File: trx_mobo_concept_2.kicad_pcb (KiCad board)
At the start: 2 copper layers, 200 x 100 mm, 416 parts, among them J301 CONN_SMA_VERT, J302 CONN2, J303 CONN_SMA_VERT, J304 CONN3, J305 CONN_SMA_VERT, J306 CONN3, J307 CONN2, J308 CONN_SMA_VERT, J309 CONN8, Q1201 BSS138, Q1301 MMBT3904, Q1302 MMBT3904, Q1303 MMBT3904, Q1601 SI2369, Q1602 BSS138, Q1603 MMBT3904, Q1604 SI2369, Q1605 BSS138, Q1606 MMBT3904, Q1701 MMBT3906, Q1702 MMBT3904, Q1703 MMBT3904, Q2101 2SC3357, Q2102 2SC3357, Q2301 2SC3357, Q301 BSS138, Q401 BSS138, Q402 BSS138, Q801 MMBT3904, Q901 MMBFJ310, Q902 MMBFJ310, Q903 MMBT3904, Q904 MMBT3904, Q905 BSS138, T2101 XFMR_RF_BIFILAR, T2102 XFMR_RF_BIFILAR, T2301 XFMR_RF_BIFILAR, T801 XFMR_RF_BIFILAR, T901 FT37-43, U1101 DG449DS-T1-E3, U1102 LMC6482, U1103 LMC6482, U1201 LM380N, U1301 ADE-1, U1701 LMC6482, U1801 AS169-73, U1802 AS169-73, U2101 AS169-73, U2102 AS169-73, U2201 ADE-1, U2301 AS169-73, U2302 AS169-73, U401 24CW640, U402 MCP4725, U403 74LVC1G00, U501 PCA9554APW, U801 ADE-1, Y2001 45.1 MHz, Y2002 45.1 MHz, Y701 12.288 MHz, Y702 12.288 MHz, Y703 12.288 MHz, Y704 12.288 MHz, Y705 12.288 MHz, Y706 12.288 MHz

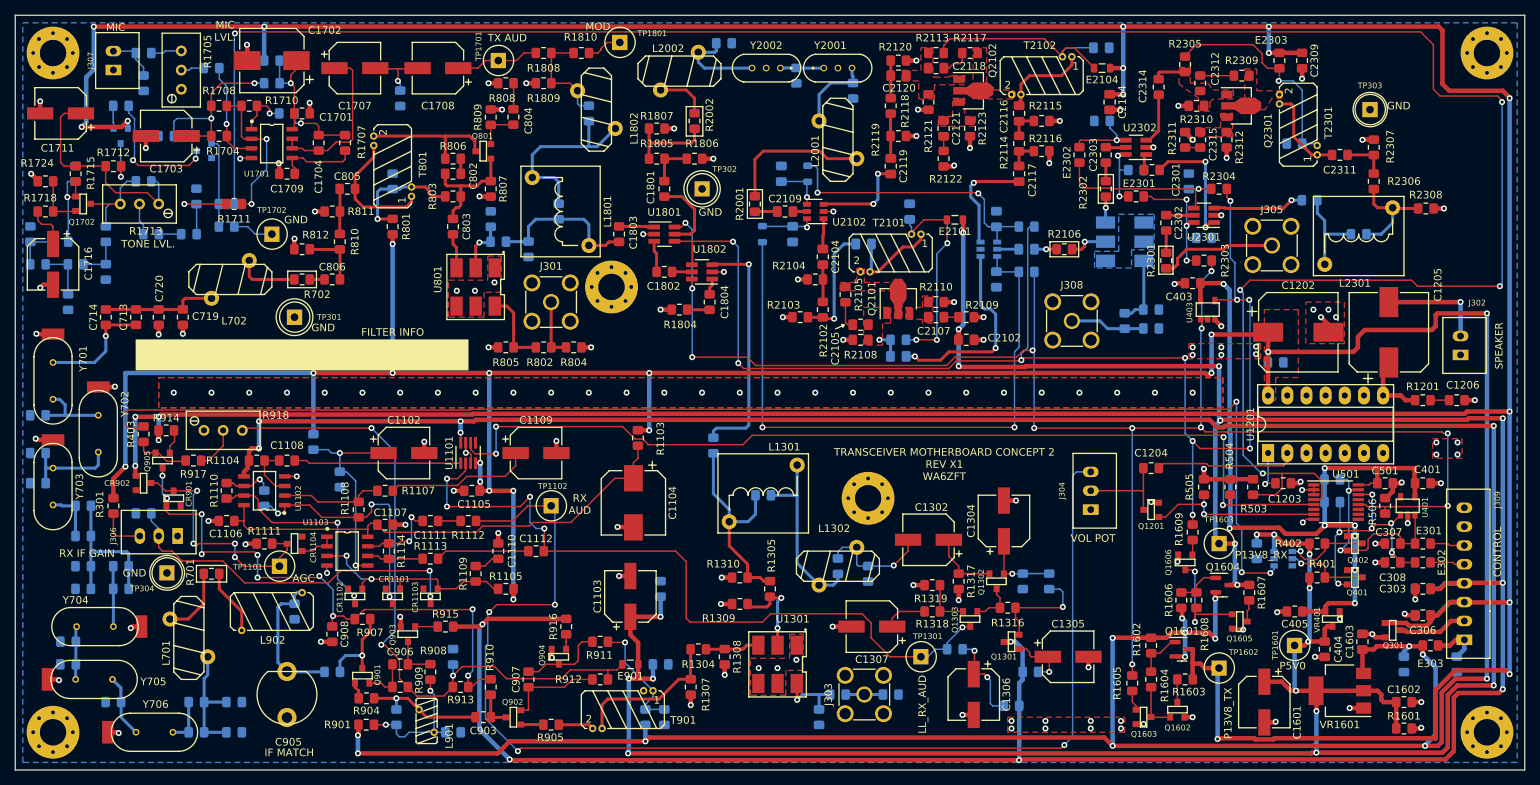
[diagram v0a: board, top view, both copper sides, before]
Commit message: trx_mobo_concept_2_B. Change design to use a dedicated 8V supply for the 2SC3357 parts. Add S-Meter connector. Change mic connector to 3 pins and add 8V sopower supply to pin 3.
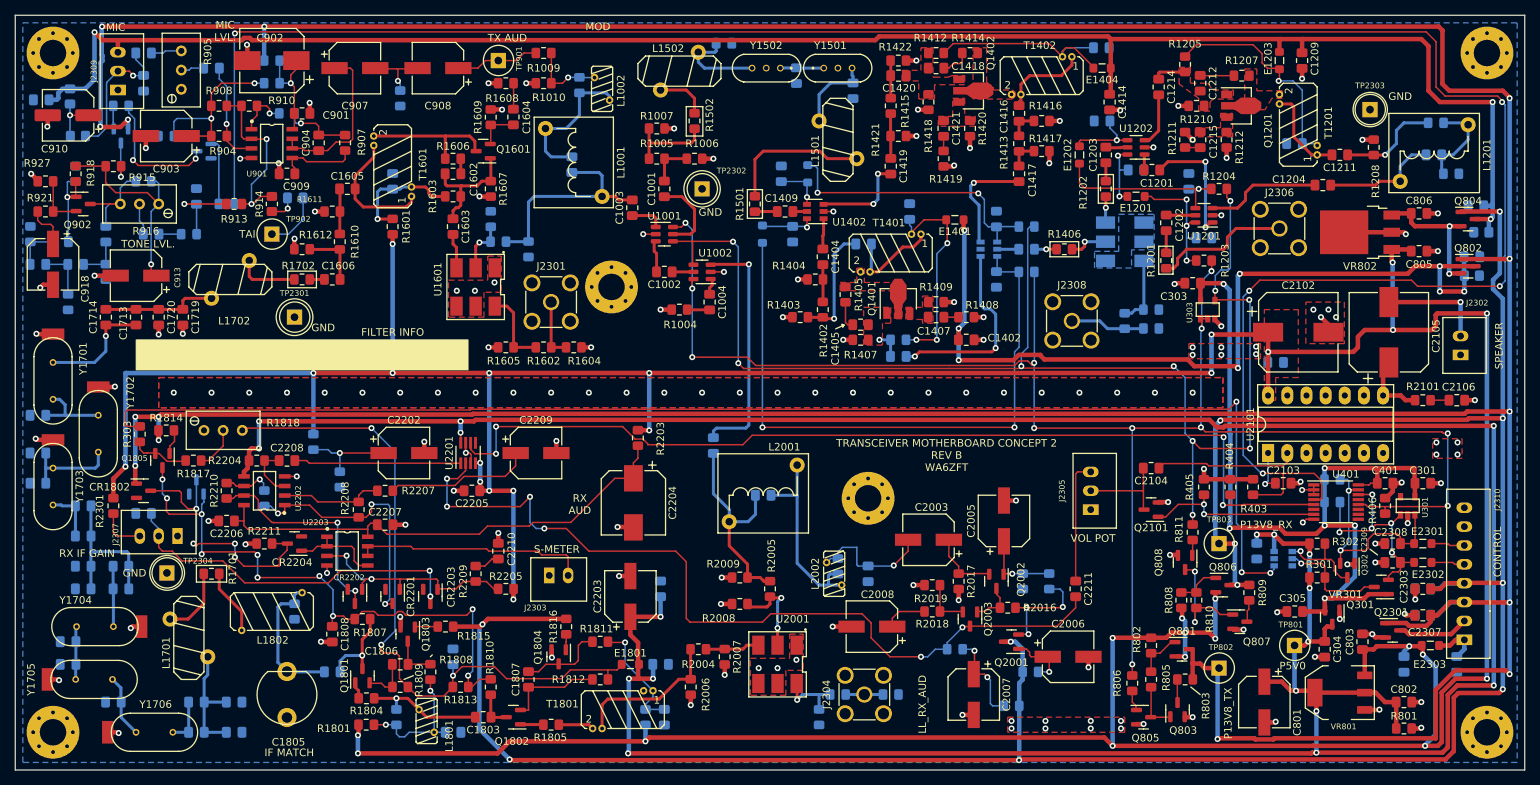
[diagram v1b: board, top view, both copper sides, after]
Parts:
- removed C1111: 4.7u, Capacitor_SMD:C_0805_2012Metric_Pad1.15x1.40mm_HandSolder
- removed J307: CONN2, mods:JST_B2B_XH_A
- removed R1112: 470, Resistor_SMD:R_0805_2012Metric_Pad1.15x1.40mm_HandSolder
- removed R1113, R1114: 10K, Resistor_SMD:R_0805_2012Metric_Pad1.15x1.40mm_HandSolder
- removed R1725: 47K, Resistor_SMD:R_0805_2012Metric_Pad1.15x1.40mm_HandSolder
- removed the R1810 at (125.0, 55.0)
- removed TP1101, TP1102, TP1301, TP1801: TESTPINTPSQ025, mods:TESTPIN
- added C2305: 0.1u, Capacitor_SMD:C_0805_2012Metric_Pad1.18x1.45mm_HandSolder, B.Cu at (53.4, 61.2)
- added C804: 0.1u, Capacitor_SMD:C_0805_2012Metric_Pad1.18x1.45mm_HandSolder, B.Cu at (243.0, 82.0)
- added C805: 4.7u, Capacitor_SMD:C_0805_2012Metric_Pad1.18x1.45mm_HandSolder, F.Cu at (236.0, 81.2)
- added C806: 4.7u, Capacitor_SMD:C_0805_2012Metric_Pad1.18x1.45mm_HandSolder, F.Cu at (236.0, 76.2)
- added C807: 0.1u, Capacitor_SMD:C_0805_2012Metric_Pad1.18x1.45mm_HandSolder, B.Cu at (243.5, 75.2)
- added C910: 22u, Capacitor_SMD:CP_Elec_6.3x5.7, F.Cu at (57.0, 63.2)
- added C911: 0.1u, Capacitor_SMD:C_0805_2012Metric_Pad1.18x1.45mm_HandSolder, B.Cu at (87.1, 74.2)
- added J2303: CONN2, mods:JST_B2B_XH_A, F.Cu at (122.0, 124.2)
- added J2309: CONN3, mods:JST_B3B_XH_A, F.Cu at (63.6, 57.4)
- added Q802: SI2369, Package_TO_SOT_SMD:SOT-23, F.Cu at (242.5, 83.2)
- added Q804: SI2369, Package_TO_SOT_SMD:SOT-23, F.Cu at (242.5, 77.0)
- added R804: 10K, Resistor_SMD:R_0805_2012Metric_Pad1.20x1.40mm_HandSolder, B.Cu at (243.0, 84.5)
- added R807: 10K, Resistor_SMD:R_0805_2012Metric_Pad1.20x1.40mm_HandSolder, B.Cu at (244.2, 78.8)
- added R911: 100, Resistor_SMD:R_0805_2012Metric_Pad1.20x1.40mm_HandSolder, B.Cu at (57.2, 60.8)
- added R912: 6.8K, Resistor_SMD:R_0805_2012Metric_Pad1.20x1.40mm_HandSolder, B.Cu at (58.3, 66.0)
- added R914: 100K, Resistor_SMD:R_0805_2012Metric_Pad1.20x1.40mm_HandSolder, F.Cu at (84.0, 75.0)
- added VR802: MC78M08CDTRKG, Package_TO_SOT_SMD:TO-252-3_TabPin2, F.Cu at (228.2, 78.8)
- C1001: renamed from C1801; footprint Capacitor_SMD:C_0805_2012Metric_Pad1.15x1.40mm_HandSolder -> Capacitor_SMD:C_0805_2012Metric_Pad1.18x1.45mm_HandSolder
- C1002: renamed from C1802; footprint Capacitor_SMD:C_0805_2012Metric_Pad1.15x1.40mm_HandSolder -> Capacitor_SMD:C_0805_2012Metric_Pad1.18x1.45mm_HandSolder
- C1003: renamed from C1803; footprint Capacitor_SMD:C_0805_2012Metric_Pad1.15x1.40mm_HandSolder -> Capacitor_SMD:C_0805_2012Metric_Pad1.18x1.45mm_HandSolder
- C1004: renamed from C1804; footprint Capacitor_SMD:C_0805_2012Metric_Pad1.15x1.40mm_HandSolder -> Capacitor_SMD:C_0805_2012Metric_Pad1.18x1.45mm_HandSolder
- C1005: renamed from C1805; footprint Capacitor_SMD:C_0805_2012Metric_Pad1.15x1.40mm_HandSolder -> Capacitor_SMD:C_0805_2012Metric_Pad1.18x1.45mm_HandSolder
- C1201: renamed from C2301; footprint Capacitor_SMD:C_0805_2012Metric_Pad1.15x1.40mm_HandSolder -> Capacitor_SMD:C_0805_2012Metric_Pad1.18x1.45mm_HandSolder
- C1202: renamed from C2302; footprint Capacitor_SMD:C_0805_2012Metric_Pad1.15x1.40mm_HandSolder -> Capacitor_SMD:C_0805_2012Metric_Pad1.18x1.45mm_HandSolder
- C1203: renamed from C2303; footprint Capacitor_SMD:C_0805_2012Metric_Pad1.15x1.40mm_HandSolder -> Capacitor_SMD:C_0805_2012Metric_Pad1.18x1.45mm_HandSolder
- C1204: renamed from C2304; footprint Capacitor_SMD:C_0805_2012Metric_Pad1.15x1.40mm_HandSolder -> Capacitor_SMD:C_0805_2012Metric_Pad1.18x1.45mm_HandSolder; moved to F.Cu
- C1205: renamed from C2305; footprint Capacitor_SMD:C_0805_2012Metric_Pad1.15x1.40mm_HandSolder -> Capacitor_SMD:C_0805_2012Metric_Pad1.18x1.45mm_HandSolder
- C1206: renamed from C2306; footprint Capacitor_SMD:C_0805_2012Metric_Pad1.15x1.40mm_HandSolder -> Capacitor_SMD:C_0805_2012Metric_Pad1.18x1.45mm_HandSolder
- C1207: renamed from C2307; footprint Capacitor_SMD:C_0805_2012Metric_Pad1.15x1.40mm_HandSolder -> Capacitor_SMD:C_0805_2012Metric_Pad1.18x1.45mm_HandSolder
- C1208: renamed from C2308; footprint Capacitor_SMD:C_0805_2012Metric_Pad1.15x1.40mm_HandSolder -> Capacitor_SMD:C_0805_2012Metric_Pad1.18x1.45mm_HandSolder
- C1209: renamed from C2309; footprint Capacitor_SMD:C_0805_2012Metric_Pad1.15x1.40mm_HandSolder -> Capacitor_SMD:C_0805_2012Metric_Pad1.18x1.45mm_HandSolder
- C1210: renamed from C2310; footprint Capacitor_SMD:C_0805_2012Metric_Pad1.15x1.40mm_HandSolder -> Capacitor_SMD:C_0805_2012Metric_Pad1.18x1.45mm_HandSolder
- C1211: renamed from C2311; footprint Capacitor_SMD:C_0805_2012Metric_Pad1.15x1.40mm_HandSolder -> Capacitor_SMD:C_0805_2012Metric_Pad1.18x1.45mm_HandSolder
- C1212: renamed from C2312; footprint Capacitor_SMD:C_0805_2012Metric_Pad1.15x1.40mm_HandSolder -> Capacitor_SMD:C_0805_2012Metric_Pad1.18x1.45mm_HandSolder
- C1213: renamed from C2313; footprint Capacitor_SMD:C_0805_2012Metric_Pad1.15x1.40mm_HandSolder -> Capacitor_SMD:C_0805_2012Metric_Pad1.18x1.45mm_HandSolder
- C1214: renamed from C2314; footprint Capacitor_SMD:C_0805_2012Metric_Pad1.15x1.40mm_HandSolder -> Capacitor_SMD:C_0805_2012Metric_Pad1.18x1.45mm_HandSolder
- C1215: renamed from C2315; footprint Capacitor_SMD:C_0805_2012Metric_Pad1.15x1.40mm_HandSolder -> Capacitor_SMD:C_0805_2012Metric_Pad1.18x1.45mm_HandSolder
- C1501: renamed from C2001; footprint Capacitor_SMD:C_0805_2012Metric_Pad1.15x1.40mm_HandSolder -> Capacitor_SMD:C_0805_2012Metric_Pad1.18x1.45mm_HandSolder
- C1502: renamed from C2002; footprint Capacitor_SMD:C_0805_2012Metric_Pad1.15x1.40mm_HandSolder -> Capacitor_SMD:C_0805_2012Metric_Pad1.18x1.45mm_HandSolder
- C1503: renamed from C2003; footprint Capacitor_SMD:C_0805_2012Metric_Pad1.15x1.40mm_HandSolder -> Capacitor_SMD:C_0805_2012Metric_Pad1.18x1.45mm_HandSolder
- C1601: renamed from C801; footprint Capacitor_SMD:C_0805_2012Metric_Pad1.15x1.40mm_HandSolder -> Capacitor_SMD:C_0805_2012Metric_Pad1.18x1.45mm_HandSolder
- C1602: renamed from C802; footprint Capacitor_SMD:C_0805_2012Metric_Pad1.15x1.40mm_HandSolder -> Capacitor_SMD:C_0805_2012Metric_Pad1.18x1.45mm_HandSolder
- C1603: renamed from C803; footprint Capacitor_SMD:C_0805_2012Metric_Pad1.15x1.40mm_HandSolder -> Capacitor_SMD:C_0805_2012Metric_Pad1.18x1.45mm_HandSolder
- C1604: renamed from C804; footprint Capacitor_SMD:C_0805_2012Metric_Pad1.15x1.40mm_HandSolder -> Capacitor_SMD:C_0805_2012Metric_Pad1.18x1.45mm_HandSolder
- C1605: renamed from C805; footprint Capacitor_SMD:C_0805_2012Metric_Pad1.15x1.40mm_HandSolder -> Capacitor_SMD:C_0805_2012Metric_Pad1.18x1.45mm_HandSolder
- C1606: renamed from C806; footprint Capacitor_SMD:C_0805_2012Metric_Pad1.15x1.40mm_HandSolder -> Capacitor_SMD:C_0805_2012Metric_Pad1.18x1.45mm_HandSolder
- C1701: renamed from C701; footprint Capacitor_SMD:C_0805_2012Metric_Pad1.15x1.40mm_HandSolder -> Capacitor_SMD:C_0805_2012Metric_Pad1.18x1.45mm_HandSolder
- C1702: renamed from C702; footprint Capacitor_SMD:C_0805_2012Metric_Pad1.15x1.40mm_HandSolder -> Capacitor_SMD:C_0805_2012Metric_Pad1.18x1.45mm_HandSolder
- C1703: renamed from C703; footprint Capacitor_SMD:C_0805_2012Metric_Pad1.15x1.40mm_HandSolder -> Capacitor_SMD:C_0805_2012Metric_Pad1.18x1.45mm_HandSolder
- C1704: renamed from C704; footprint Capacitor_SMD:C_0805_2012Metric_Pad1.15x1.40mm_HandSolder -> Capacitor_SMD:C_0805_2012Metric_Pad1.18x1.45mm_HandSolder
- C1705: renamed from C705; footprint Capacitor_SMD:C_0805_2012Metric_Pad1.15x1.40mm_HandSolder -> Capacitor_SMD:C_0805_2012Metric_Pad1.18x1.45mm_HandSolder
- C1706: renamed from C706; footprint Capacitor_SMD:C_0805_2012Metric_Pad1.15x1.40mm_HandSolder -> Capacitor_SMD:C_0805_2012Metric_Pad1.18x1.45mm_HandSolder
- C1707: renamed from C707; footprint Capacitor_SMD:C_0805_2012Metric_Pad1.15x1.40mm_HandSolder -> Capacitor_SMD:C_0805_2012Metric_Pad1.18x1.45mm_HandSolder
- C1708: renamed from C708; footprint Capacitor_SMD:C_0805_2012Metric_Pad1.15x1.40mm_HandSolder -> Capacitor_SMD:C_0805_2012Metric_Pad1.18x1.45mm_HandSolder
- C1709: renamed from C709; footprint Capacitor_SMD:C_0805_2012Metric_Pad1.15x1.40mm_HandSolder -> Capacitor_SMD:C_0805_2012Metric_Pad1.18x1.45mm_HandSolder
- C1710: renamed from C710; footprint Capacitor_SMD:C_0805_2012Metric_Pad1.15x1.40mm_HandSolder -> Capacitor_SMD:C_0805_2012Metric_Pad1.18x1.45mm_HandSolder
- C1711: renamed from C711; footprint Capacitor_SMD:C_0805_2012Metric_Pad1.15x1.40mm_HandSolder -> Capacitor_SMD:C_0805_2012Metric_Pad1.18x1.45mm_HandSolder
- C1712: renamed from C712; footprint Capacitor_SMD:C_0805_2012Metric_Pad1.15x1.40mm_HandSolder -> Capacitor_SMD:C_0805_2012Metric_Pad1.18x1.45mm_HandSolder
- C1713: renamed from C713; footprint Capacitor_SMD:C_0805_2012Metric_Pad1.15x1.40mm_HandSolder -> Capacitor_SMD:C_0805_2012Metric_Pad1.18x1.45mm_HandSolder
- C1714: renamed from C714; footprint Capacitor_SMD:C_0805_2012Metric_Pad1.15x1.40mm_HandSolder -> Capacitor_SMD:C_0805_2012Metric_Pad1.18x1.45mm_HandSolder
- C1715: renamed from C715; footprint Capacitor_SMD:C_0805_2012Metric_Pad1.15x1.40mm_HandSolder -> Capacitor_SMD:C_0805_2012Metric_Pad1.18x1.45mm_HandSolder
- C1716: renamed from C716; footprint Capacitor_SMD:C_0805_2012Metric_Pad1.15x1.40mm_HandSolder -> Capacitor_SMD:C_0805_2012Metric_Pad1.18x1.45mm_HandSolder
- C1717: renamed from C717; footprint Capacitor_SMD:C_0805_2012Metric_Pad1.15x1.40mm_HandSolder -> Capacitor_SMD:C_0805_2012Metric_Pad1.18x1.45mm_HandSolder
- C1718: renamed from C718; footprint Capacitor_SMD:C_0805_2012Metric_Pad1.15x1.40mm_HandSolder -> Capacitor_SMD:C_0805_2012Metric_Pad1.18x1.45mm_HandSolder
- C1719: renamed from C719; footprint Capacitor_SMD:C_0805_2012Metric_Pad1.15x1.40mm_HandSolder -> Capacitor_SMD:C_0805_2012Metric_Pad1.18x1.45mm_HandSolder
- C1720: renamed from C720; footprint Capacitor_SMD:C_0805_2012Metric_Pad1.15x1.40mm_HandSolder -> Capacitor_SMD:C_0805_2012Metric_Pad1.18x1.45mm_HandSolder
- C1801: renamed from C901; footprint Capacitor_SMD:C_0805_2012Metric_Pad1.15x1.40mm_HandSolder -> Capacitor_SMD:C_0805_2012Metric_Pad1.18x1.45mm_HandSolder
- C1802: renamed from C902; footprint Capacitor_SMD:C_0805_2012Metric_Pad1.15x1.40mm_HandSolder -> Capacitor_SMD:C_0805_2012Metric_Pad1.18x1.45mm_HandSolder
- C1803: renamed from C903; footprint Capacitor_SMD:C_0805_2012Metric_Pad1.15x1.40mm_HandSolder -> Capacitor_SMD:C_0805_2012Metric_Pad1.18x1.45mm_HandSolder
- C1804: renamed from C904; footprint Capacitor_SMD:C_0805_2012Metric_Pad1.15x1.40mm_HandSolder -> Capacitor_SMD:C_0805_2012Metric_Pad1.18x1.45mm_HandSolder
- C1806: renamed from C906; footprint Capacitor_SMD:C_0805_2012Metric_Pad1.15x1.40mm_HandSolder -> Capacitor_SMD:C_0805_2012Metric_Pad1.18x1.45mm_HandSolder
- C1807: renamed from C907; footprint Capacitor_SMD:C_0805_2012Metric_Pad1.15x1.40mm_HandSolder -> Capacitor_SMD:C_0805_2012Metric_Pad1.18x1.45mm_HandSolder
- C1808: renamed from C908; footprint Capacitor_SMD:C_0805_2012Metric_Pad1.15x1.40mm_HandSolder -> Capacitor_SMD:C_0805_2012Metric_Pad1.18x1.45mm_HandSolder
- C1809: renamed from C909; footprint Capacitor_SMD:C_0805_2012Metric_Pad1.15x1.40mm_HandSolder -> Capacitor_SMD:C_0805_2012Metric_Pad1.18x1.45mm_HandSolder
- C1810: renamed from C910; footprint Capacitor_SMD:C_0805_2012Metric_Pad1.15x1.40mm_HandSolder -> Capacitor_SMD:C_0805_2012Metric_Pad1.18x1.45mm_HandSolder
- C2001: renamed from C1308; footprint Capacitor_SMD:C_0805_2012Metric_Pad1.15x1.40mm_HandSolder -> Capacitor_SMD:C_0805_2012Metric_Pad1.18x1.45mm_HandSolder
- C2002: renamed from C1301; footprint Capacitor_SMD:C_0805_2012Metric_Pad1.15x1.40mm_HandSolder -> Capacitor_SMD:C_0805_2012Metric_Pad1.18x1.45mm_HandSolder
- C2004: renamed from C1303; footprint Capacitor_SMD:C_0805_2012Metric_Pad1.15x1.40mm_HandSolder -> Capacitor_SMD:C_0805_2012Metric_Pad1.18x1.45mm_HandSolder
- C2101: renamed from C1201; footprint Capacitor_SMD:C_0805_2012Metric_Pad1.15x1.40mm_HandSolder -> Capacitor_SMD:C_0805_2012Metric_Pad1.18x1.45mm_HandSolder
- C2103: renamed from C1203; footprint Capacitor_SMD:C_0805_2012Metric_Pad1.15x1.40mm_HandSolder -> Capacitor_SMD:C_0805_2012Metric_Pad1.18x1.45mm_HandSolder
- C2104: renamed from C1204; footprint Capacitor_SMD:C_0805_2012Metric_Pad1.15x1.40mm_HandSolder -> Capacitor_SMD:C_0805_2012Metric_Pad1.18x1.45mm_HandSolder
- C2106: renamed from C1206; footprint Capacitor_SMD:C_0805_2012Metric_Pad1.15x1.40mm_HandSolder -> Capacitor_SMD:C_0805_2012Metric_Pad1.18x1.45mm_HandSolder
- C2201: renamed from C1101; footprint Capacitor_SMD:C_0805_2012Metric_Pad1.15x1.40mm_HandSolder -> Capacitor_SMD:C_0805_2012Metric_Pad1.18x1.45mm_HandSolder
- C2205: renamed from C1105; footprint Capacitor_SMD:C_0805_2012Metric_Pad1.15x1.40mm_HandSolder -> Capacitor_SMD:C_0805_2012Metric_Pad1.18x1.45mm_HandSolder
- C2206: renamed from C1106; footprint Capacitor_SMD:C_0805_2012Metric_Pad1.15x1.40mm_HandSolder -> Capacitor_SMD:C_0805_2012Metric_Pad1.18x1.45mm_HandSolder
- C2207: renamed from C1107; footprint Capacitor_SMD:C_0805_2012Metric_Pad1.15x1.40mm_HandSolder -> Capacitor_SMD:C_0805_2012Metric_Pad1.18x1.45mm_HandSolder
- C2208: renamed from C1108; footprint Capacitor_SMD:C_0805_2012Metric_Pad1.15x1.40mm_HandSolder -> Capacitor_SMD:C_0805_2012Metric_Pad1.18x1.45mm_HandSolder
- C2210: renamed from C1110; footprint Capacitor_SMD:C_0805_2012Metric_Pad1.15x1.40mm_HandSolder -> Capacitor_SMD:C_0805_2012Metric_Pad1.18x1.45mm_HandSolder
- C2211: renamed from C1112; footprint Capacitor_SMD:C_0805_2012Metric_Pad1.15x1.40mm_HandSolder -> Capacitor_SMD:C_0805_2012Metric_Pad1.18x1.45mm_HandSolder
- C2301: renamed from C301; footprint Capacitor_SMD:C_0805_2012Metric_Pad1.15x1.40mm_HandSolder -> Capacitor_SMD:C_0805_2012Metric_Pad1.18x1.45mm_HandSolder
- C2302: renamed from C302; footprint Capacitor_SMD:C_0805_2012Metric_Pad1.15x1.40mm_HandSolder -> Capacitor_SMD:C_0805_2012Metric_Pad1.18x1.45mm_HandSolder
- C2303: renamed from C303; footprint Capacitor_SMD:C_0805_2012Metric_Pad1.15x1.40mm_HandSolder -> Capacitor_SMD:C_0805_2012Metric_Pad1.18x1.45mm_HandSolder
- C2304: renamed from C304; footprint Capacitor_SMD:C_0805_2012Metric_Pad1.15x1.40mm_HandSolder -> Capacitor_SMD:C_0805_2012Metric_Pad1.18x1.45mm_HandSolder
- C2306: renamed from C305; footprint Capacitor_SMD:C_0805_2012Metric_Pad1.15x1.40mm_HandSolder -> Capacitor_SMD:C_0805_2012Metric_Pad1.18x1.45mm_HandSolder
- C2307: renamed from C306; footprint Capacitor_SMD:C_0805_2012Metric_Pad1.15x1.40mm_HandSolder -> Capacitor_SMD:C_0805_2012Metric_Pad1.18x1.45mm_HandSolder
- C2308: renamed from C307; footprint Capacitor_SMD:C_0805_2012Metric_Pad1.15x1.40mm_HandSolder -> Capacitor_SMD:C_0805_2012Metric_Pad1.18x1.45mm_HandSolder
- C2309: renamed from C308; footprint Capacitor_SMD:C_0805_2012Metric_Pad1.15x1.40mm_HandSolder -> Capacitor_SMD:C_0805_2012Metric_Pad1.18x1.45mm_HandSolder
- C2310: renamed from C309; footprint Capacitor_SMD:C_0805_2012Metric_Pad1.15x1.40mm_HandSolder -> Capacitor_SMD:C_0805_2012Metric_Pad1.18x1.45mm_HandSolder
- C2311: renamed from C310; footprint Capacitor_SMD:C_0805_2012Metric_Pad1.15x1.40mm_HandSolder -> Capacitor_SMD:C_0805_2012Metric_Pad1.18x1.45mm_HandSolder
- C301: renamed from C401; footprint Capacitor_SMD:C_0805_2012Metric_Pad1.15x1.40mm_HandSolder -> Capacitor_SMD:C_0805_2012Metric_Pad1.18x1.45mm_HandSolder
- C302: renamed from C402; footprint Capacitor_SMD:C_0805_2012Metric_Pad1.15x1.40mm_HandSolder -> Capacitor_SMD:C_0805_2012Metric_Pad1.18x1.45mm_HandSolder
- C303: renamed from C403; footprint Capacitor_SMD:C_0805_2012Metric_Pad1.15x1.40mm_HandSolder -> Capacitor_SMD:C_0805_2012Metric_Pad1.18x1.45mm_HandSolder
- C304: renamed from C404; footprint Capacitor_SMD:C_0805_2012Metric_Pad1.15x1.40mm_HandSolder -> Capacitor_SMD:C_0805_2012Metric_Pad1.18x1.45mm_HandSolder
- C305: renamed from C405; footprint Capacitor_SMD:C_0805_2012Metric_Pad1.15x1.40mm_HandSolder -> Capacitor_SMD:C_0805_2012Metric_Pad1.18x1.45mm_HandSolder
- C401: renamed from C501; footprint Capacitor_SMD:C_0805_2012Metric_Pad1.15x1.40mm_HandSolder -> Capacitor_SMD:C_0805_2012Metric_Pad1.18x1.45mm_HandSolder
- C802: renamed from C1602; footprint Capacitor_SMD:C_0805_2012Metric_Pad1.15x1.40mm_HandSolder -> Capacitor_SMD:C_0805_2012Metric_Pad1.18x1.45mm_HandSolder
- C901: renamed from C1701; footprint Capacitor_SMD:C_0805_2012Metric_Pad1.15x1.40mm_HandSolder -> Capacitor_SMD:C_0805_2012Metric_Pad1.18x1.45mm_HandSolder
- C904: renamed from C1704; footprint Capacitor_SMD:C_0805_2012Metric_Pad1.15x1.40mm_HandSolder -> Capacitor_SMD:C_0805_2012Metric_Pad1.18x1.45mm_HandSolder
- C905: renamed from C1705; footprint Capacitor_SMD:C_0805_2012Metric_Pad1.15x1.40mm_HandSolder -> Capacitor_SMD:C_0805_2012Metric_Pad1.18x1.45mm_HandSolder
- C906: renamed from C1706; footprint Capacitor_SMD:C_0805_2012Metric_Pad1.15x1.40mm_HandSolder -> Capacitor_SMD:C_0805_2012Metric_Pad1.18x1.45mm_HandSolder
- C909: renamed from C1709; footprint Capacitor_SMD:C_0805_2012Metric_Pad1.15x1.40mm_HandSolder -> Capacitor_SMD:C_0805_2012Metric_Pad1.18x1.45mm_HandSolder
- C912: renamed from C1710; footprint Capacitor_SMD:C_0805_2012Metric_Pad1.15x1.40mm_HandSolder -> Capacitor_SMD:C_0805_2012Metric_Pad1.18x1.45mm_HandSolder
- C914: renamed from C1712; footprint Capacitor_SMD:C_0805_2012Metric_Pad1.15x1.40mm_HandSolder -> Capacitor_SMD:C_0805_2012Metric_Pad1.18x1.45mm_HandSolder
- C915: renamed from C1713; footprint Capacitor_SMD:C_0805_2012Metric_Pad1.15x1.40mm_HandSolder -> Capacitor_SMD:C_0805_2012Metric_Pad1.18x1.45mm_HandSolder
- C916: renamed from C1714; footprint Capacitor_SMD:C_0805_2012Metric_Pad1.15x1.40mm_HandSolder -> Capacitor_SMD:C_0805_2012Metric_Pad1.18x1.45mm_HandSolder
- C917: renamed from C1715; footprint Capacitor_SMD:C_0805_2012Metric_Pad1.15x1.40mm_HandSolder -> Capacitor_SMD:C_0805_2012Metric_Pad1.18x1.45mm_HandSolder
- C919: renamed from C1717; footprint Capacitor_SMD:C_0805_2012Metric_Pad1.15x1.40mm_HandSolder -> Capacitor_SMD:C_0805_2012Metric_Pad1.18x1.45mm_HandSolder
- CR1801: renamed from CR901; footprint mods:SOT23-3-SAR -> mods:SOT23-3-SAR-V2; moved to B.Cu
- CR1802: renamed from CR902; footprint mods:SOT23-3-SAR -> mods:SOT23-3-SAR-V2
- CR2201: renamed from CR1101; footprint mods:SOT23-3-SAR -> mods:SOT23-3-SAR-V2
- CR2202: renamed from CR1102; footprint mods:SOT23-3-SAR -> mods:SOT23-3-SAR-V2
- CR2203: renamed from CR1103; footprint mods:SOT23-3-SAR -> mods:SOT23-3-SAR-V2
- CR2204: renamed from CR1104; footprint mods:SOT23-3-SAR -> mods:SOT23-3-SAR-V2
- E1201: renamed from E2301; footprint Inductor_SMD:L_0805_2012Metric_Pad1.15x1.40mm_HandSolder -> Inductor_SMD:L_0805_2012Metric_Pad1.05x1.20mm_HandSolder
- E1202: renamed from E2302; footprint Inductor_SMD:L_0805_2012Metric_Pad1.15x1.40mm_HandSolder -> Inductor_SMD:L_0805_2012Metric_Pad1.05x1.20mm_HandSolder
- E1203: renamed from E2303; footprint Inductor_SMD:L_0805_2012Metric_Pad1.15x1.40mm_HandSolder -> Inductor_SMD:L_0805_2012Metric_Pad1.05x1.20mm_HandSolder
- E1401: renamed from E2101; footprint Inductor_SMD:L_0805_2012Metric -> Inductor_SMD:L_0805_2012Metric_Pad1.05x1.20mm_HandSolder
- E1402: renamed from E2102; footprint Inductor_SMD:L_0805_2012Metric -> Inductor_SMD:L_0805_2012Metric_Pad1.05x1.20mm_HandSolder
- E1403: renamed from E2103; footprint Inductor_SMD:L_0805_2012Metric -> Inductor_SMD:L_0805_2012Metric_Pad1.05x1.20mm_HandSolder
- E1404: renamed from E2104; footprint Inductor_SMD:L_0805_2012Metric -> Inductor_SMD:L_0805_2012Metric_Pad1.05x1.20mm_HandSolder
- E1801: renamed from E901; value GZ2012U601TF -> FB0805; footprint Inductor_SMD:L_0805_2012Metric -> Inductor_SMD:L_0805_2012Metric_Pad1.05x1.20mm_HandSolder
- E2301: renamed from E301; footprint Inductor_SMD:L_0805_2012Metric_Pad1.15x1.40mm_HandSolder -> Inductor_SMD:L_0805_2012Metric_Pad1.05x1.20mm_HandSolder
- E2302: renamed from E302; footprint Inductor_SMD:L_0805_2012Metric_Pad1.15x1.40mm_HandSolder -> Inductor_SMD:L_0805_2012Metric_Pad1.05x1.20mm_HandSolder
- E2303: renamed from E303; footprint Inductor_SMD:L_0805_2012Metric_Pad1.15x1.40mm_HandSolder -> Inductor_SMD:L_0805_2012Metric_Pad1.05x1.20mm_HandSolder
- L1002: renamed from L1802; footprint mods:TOROID_T37_VERT -> mods:IND_Handwound_FT23
- L2002: renamed from L1302; footprint mods:TOROID_T37_VERT -> mods:IND_Handwound_FT23
- Q1601: renamed from Q801; footprint mods:SOT23-3-SAR -> mods:SOT23-3-SAR-V2
- Q1801: renamed from Q901; footprint mods:SOT23-3-SAR -> mods:SOT23-3-SAR-V2
- Q1802: renamed from Q902; footprint mods:SOT23-3-SAR -> mods:SOT23-3-SAR-V2
- Q1803: renamed from Q903; footprint mods:SOT23-3-SAR -> mods:SOT23-3-SAR-V2
- Q1804: renamed from Q904; footprint mods:SOT23-3-SAR -> mods:SOT23-3-SAR-V2
- Q1805: renamed from Q905; footprint mods:SOT23-3-SAR -> Package_TO_SOT_SMD:SOT-23
- Q2001: renamed from Q1301; footprint mods:SOT23-3-SAR -> mods:SOT23-3-SAR-V2
- Q2002: renamed from Q1302; footprint mods:SOT23-3-SAR -> mods:SOT23-3-SAR-V2
- Q2003: renamed from Q1303; footprint mods:SOT23-3-SAR -> mods:SOT23-3-SAR-V2
- Q2101: renamed from Q1201; footprint mods:SOT23-3-SAR -> Package_TO_SOT_SMD:SOT-23
- Q2301: renamed from Q301; footprint mods:SOT23-3-SAR -> Package_TO_SOT_SMD:SOT-23
- Q301: renamed from Q401; footprint mods:SOT23-3-SAR -> Package_TO_SOT_SMD:SOT-23
- Q302: renamed from Q402; footprint mods:SOT23-3-SAR -> Package_TO_SOT_SMD:SOT-23
- Q803: renamed from Q1602; footprint mods:SOT23-3-SAR -> Package_TO_SOT_SMD:SOT-23
- Q805: renamed from Q1603; footprint mods:SOT23-3-SAR -> mods:SOT23-3-SAR-V2
- Q807: renamed from Q1605; footprint mods:SOT23-3-SAR -> Package_TO_SOT_SMD:SOT-23
- Q808: renamed from Q1606; footprint mods:SOT23-3-SAR -> mods:SOT23-3-SAR-V2
- Q901: renamed from Q1701; footprint mods:SOT23-3-SAR -> mods:SOT23-3-SAR-V2
- Q902: renamed from Q1702; footprint mods:SOT23-3-SAR -> mods:SOT23-3-SAR-V2
- Q903: renamed from Q1703; footprint mods:SOT23-3-SAR -> mods:SOT23-3-SAR-V2
- R1205: renamed from R2305; value 2K -> 1.1K
- R1206: renamed from R2306; moved to B.Cu
- R1207: renamed from R2309; value 330 -> 910
- R1209: renamed from R2308; moved to B.Cu
- R1211: renamed from R2311; value 22 -> 10
- R1401: renamed from R2101; value 2K -> 1.1K
- R1412: renamed from R2113; value 2K -> 1.1K
- U1001: renamed from U1801; footprint Package_TO_SOT_SMD:SOT-23-6_Handsoldering -> Package_TO_SOT_SMD:SOT-23-6
- U1002: renamed from U1802; footprint Package_TO_SOT_SMD:SOT-23-6_Handsoldering -> Package_TO_SOT_SMD:SOT-23-6
- U1201: renamed from U2301; footprint Package_TO_SOT_SMD:SOT-23-6_Handsoldering -> Package_TO_SOT_SMD:SOT-23-6
- U1202: renamed from U2302; footprint Package_TO_SOT_SMD:SOT-23-6_Handsoldering -> Package_TO_SOT_SMD:SOT-23-6
- VR301: renamed from VR401; footprint mods:SOT23-3-SAR -> mods:SOT23-3-SAR-V2
- VR801: renamed from VR1601; footprint Package_TO_SOT_SMD:SOT-223-3_TabPin2 -> mods:SOT-223-TAB-2-SAR
- moved C2211 71.7 mm to (190.5, 126.0), turned to -90 degrees
- moved C913 23.7 mm to (66.0, 84.5)
- moved L1201 14.9 mm to (238.0, 68.5)
- moved C1213 14.5 mm to (238.0, 68.5)
- moved R1206 11.3 mm to (238.2, 64.2), turned to 180 degrees
- moved L1001 6.73 mm to (123.8, 69.5)
- moved C1005 6.45 mm to (123.8, 69.8)
- moved R1209 5.69 mm to (240.2, 71.0)
- moved R1008 3.95 mm to (124.8, 59.2)
- moved C1003 3.91 mm to (131.8, 75.5), turned to 90 degrees
- moved Q301 3.72 mm to (231.0, 125.8), turned to 180 degrees
- moved Q302 3.70 mm to (226.5, 123.6)
- moved CR1801 3.35 mm to (74.0, 112.5), turned to 90 degrees
- moved C1204 2.66 mm to (223.2, 72.5)
- moved J2306 2.46 mm to (217.5, 78.2)
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- renumbered C2101 to C1401, C2102 to C1402, C2103 to C1403, C2104 to C1404, C2105 to C1405, C2106 to C1406, C2107 to C1407, C2108 to C1408, C2109 to C1409, C2110 to C1410, C2111 to C1411, C2112 to C1412, C2113 to C1413, C2114 to C1414, C2115 to C1415, C2116 to C1416, C2117 to C1417, C2118 to C1418, C2119 to C1419, C2120 to C1420, C2121 to C1421, C905 to C1805, C1302 to C2003, C1304 to C2005, C1305 to C2006, C1306 to C2007, C1307 to C2008, C1202 to C2102, C1205 to C2105, C1102 to C2202, C1103 to C2203, C1104 to C2204, C1109 to C2209, C1601 to C801, C1603 to C803, C1702 to C902, C1703 to C903, C1707 to C907, C1708 to C908, C1711 to C913, C1716 to C918, J301 to J2301, J302 to J2302, J303 to J2304, J304 to J2305, J305 to J2306, J306 to J2307, J308 to J2308, J309 to J2310, L1801 to L1001, L2301 to L1201, L2001 to L1501, L2002 to L1502, L701 to L1701, L702 to L1702, L901 to L1801, L902 to L1802, L1301 to L2001, MH301 to MH2301, MH302 to MH2302, MH303 to MH2303, MH304 to MH2304, MH305 to MH2305, MH306 to MH2306, Q2301 to Q1201, Q2101 to Q1401, Q2102 to Q1402, Q1601 to Q801, Q1604 to Q806, R1801 to R1001, R1802 to R1002, R1803 to R1003, R1804 to R1004, R1805 to R1005, R1806 to R1006, R1807 to R1007, R1811 to R1008, R1808 to R1009, R1809 to R1010, R2301 to R1201, R2302 to R1202, R2303 to R1203, R2304 to R1204, R2307 to R1208, R2310 to R1210, R2312 to R1212, R2201 to R1301, R2202 to R1302, R2203 to R1303, R2102 to R1402, R2103 to R1403, R2104 to R1404, R2105 to R1405, R2106 to R1406, R2108 to R1407, R2109 to R1408, R2110 to R1409, R2111 to R1410, R2112 to R1411, R2114 to R1413, R2117 to R1414, R2118 to R1415, R2115 to R1416, R2116 to R1417, R2121 to R1418, R2122 to R1419, R2123 to R1420, R2119 to R1421, R2120 to R1422, R2001 to R1501, R2002 to R1502, R801 to R1601, R802 to R1602, R803 to R1603, R804 to R1604, R805 to R1605, R806 to R1606, R807 to R1607, R808 to R1608, R809 to R1609, R810 to R1610, R811 to R1611, R812 to R1612, R701 to R1701, R702 to R1702, R901 to R1801, R902 to R1802, R903 to R1803, R904 to R1804, R905 to R1805, R906 to R1806, R907 to R1807, R908 to R1808, R909 to R1809, R910 to R1810, R911 to R1811, R912 to R1812, R913 to R1813, R914 to R1814, R915 to R1815, R916 to R1816, R917 to R1817, R918 to R1818, R1301 to R2001, R1302 to R2002, R1303 to R2003, R1304 to R2004, R1305 to R2005, R1307 to R2006, R1308 to R2007, R1309 to R2008, R1310 to R2009, R1306 to R2010, R1311 to R2011, R1312 to R2012, R1313 to R2013, R1314 to R2014, R1315 to R2015, R1316 to R2016, R1317 to R2017, R1318 to R2018, R1319 to R2019, R1201 to R2101, R1101 to R2201, R1102 to R2202, R1103 to R2203, R1104 to R2204, R1105 to R2205, R1106 to R2206, R1107 to R2207, R1108 to R2208, R1109 to R2209, R1110 to R2210, R1111 to R2211, R301 to R2301, R401 to R301, R402 to R302, R403 to R303, R501 to R401, R502 to R402, R503 to R403, R504 to R404, R505 to R405, R506 to R406, R1601 to R801, R1602 to R802, R1603 to R803, R1604 to R805, R1605 to R806, R1606 to R808, R1607 to R809, R1608 to R810, R1609 to R811, R1701 to R901, R1702 to R902, R1703 to R903, R1704 to R904, R1705 to R905, R1706 to R906, R1707 to R907, R1708 to R908, R1709 to R909, R1710 to R910, R1711 to R913, R1712 to R915, R1713 to R916, R1714 to R917, R1715 to R918, R1716 to R919, R1717 to R920, R1718 to R921, R1719 to R922, R1720 to R923, R1721 to R924, R1722 to R925, R1723 to R926, R1724 to R927, T2301 to T1201, T2101 to T1401, T2102 to T1402, T801 to T1601, T901 to T1801, TP301 to TP2301, TP302 to TP2302, TP303 to TP2303, TP304 to TP2304, TP1601 to TP801, TP1602 to TP802, TP1603 to TP803, TP1701 to TP901, TP1702 to TP902, U2201 to U1301, U2101 to U1401, U2102 to U1402, U801 to U1601, U1301 to U2001, U1201 to U2101, U1101 to U2201, U1102 to U2202, U1103 to U2203, U401 to U301, U402 to U302, U403 to U303, U501 to U401, U1701 to U901, Y2001 to Y1501, Y2002 to Y1502, Y701 to Y1701, Y702 to Y1702, Y703 to Y1703, Y704 to Y1704, Y705 to Y1705, Y706 to Y1706
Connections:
- C1209 pad 1: /top/P13V8_TX -> /top/connectors/P8V0_TX
- C1402 pad 1: /top/P13V8_RX -> /top/radio/rf_45r1_mic_amp_tune_osc/if_45r1_mic_amp_tune_osc/P8V0_RX
- C1414 pad 1: /top/P13V8_TX -> /top/connectors/P8V0_TX
- C2211 pad 1: Net-(C1112-Pad1) -> /top/RX_AUDIO_TOP
- CR1801 pad 2: (no net) -> unconnected-(CR1801-Pad2)
- CR1802 pad 2: (no net) -> unconnected-(CR1802-Pad2)
- CR2201 pad 2: (no net) -> unconnected-(CR2201-Pad2)
- CR2202 pad 2: (no net) -> unconnected-(CR2202-Pad2)
- CR2203 pad 2: (no net) -> unconnected-(CR2203-Pad2)
- CR2204 pad 1: Net-(CR1104-Pad1) -> Net-(CR2204-Pad1)
- CR2204 pad 2: (no net) -> unconnected-(CR2204-Pad2)
- E1203 pad 1: /top/P13V8_TX -> /top/connectors/P8V0_TX
- E1401 pad 1: /top/P13V8_RX -> /top/radio/rf_45r1_mic_amp_tune_osc/if_45r1_mic_amp_tune_osc/P8V0_RX
- E1404 pad 1: /top/P13V8_TX -> /top/connectors/P8V0_TX
- U2203 pad 1: Net-(CR1104-Pad1) -> Net-(CR2204-Pad1)
- U2203 pad 2: Net-(CR1104-Pad1) -> Net-(CR2204-Pad1)
- U2203 pad 5: /top/radio/prod_det_tx_mix/agc/APBIAS -> Net-(CR2204-Pad1)
- U2203 pad 6: Net-(R1113-Pad1) -> /top/S_METER
- U2203 pad 7: Net-(C1111-Pad2) -> /top/S_METER
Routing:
- net /top/connectors/P8V0_TX: track 0.00 -> 240.4 mm, vias 0 -> 3
- net /top/RX_AUDIO_TOP: track 165.1 -> 16.3 mm, vias 4 -> 0
- net /top/radio/rf_45r1_mic_amp_tune_osc/if_45r1_mic_amp_tune_osc/P8V0_RX: track 0.00 -> 114.0 mm, vias 0 -> 8
- net /top/S_METER: track 0.00 -> 30.9 mm
- net /top/P13V8_RX: track 370.7 -> 341.2 mm, vias 14 -> 11
- net Net-(C806-Pad1): track 0.00 -> 18.6 mm, vias 0 -> 2
- net /top/P13V8_TX: track 600.7 -> 583.9 mm, vias 18 -> 14
- net /top/radio/prod_det_tx_mix/agc/APBIAS: track 27.4 -> 12.0 mm, vias 2 -> 1
- net /top/radio/prod_det_tx_mix/agc/LL_RX_AUDIO: track 98.7 -> 113.4 mm, vias 5 -> 6
- net /top/P13V8: track 575.6 -> 589.0 mm, vias 30 -> 32
- net GND: track 166.1 -> 179.1 mm, vias 160 -> 163
- net Net-(C1112-Pad1): track 12.4 -> 0.00 mm
- net Net-(CR2204-Pad1): track 0.00 -> 12.2 mm
- net /top/TX_AUDIO_IN: track 6.48 -> 18.4 mm, vias 0 -> 1
- net Net-(C1111-Pad2): track 10.8 -> 0.00 mm, vias 2 -> 0
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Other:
- board text added: "S-METER"
- board text added: "TAI"
- board text added: "TRANSCEIVER MOTHERBOARD CONCEPT 2 REV B WA6ZFT"
- board text removed: "AGC"
- board text removed: "TRANSCEIVER MOTHERBOARD CONCEPT 2 REV X1 WA6ZFT"
